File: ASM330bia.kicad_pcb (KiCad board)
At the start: 2 copper layers, 14 x 19.5 mm, 9 parts, among them J1 Conn_01x06_Pin, U1 ASM330LHH

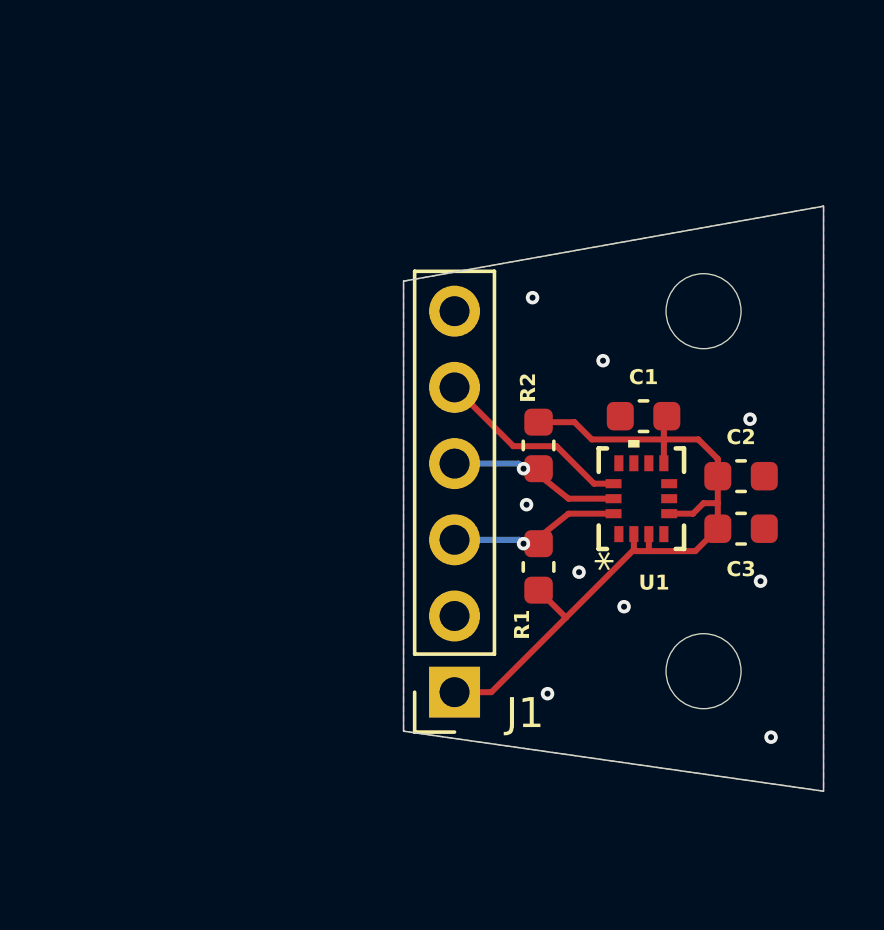
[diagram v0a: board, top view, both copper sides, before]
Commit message: alteração do furo passante
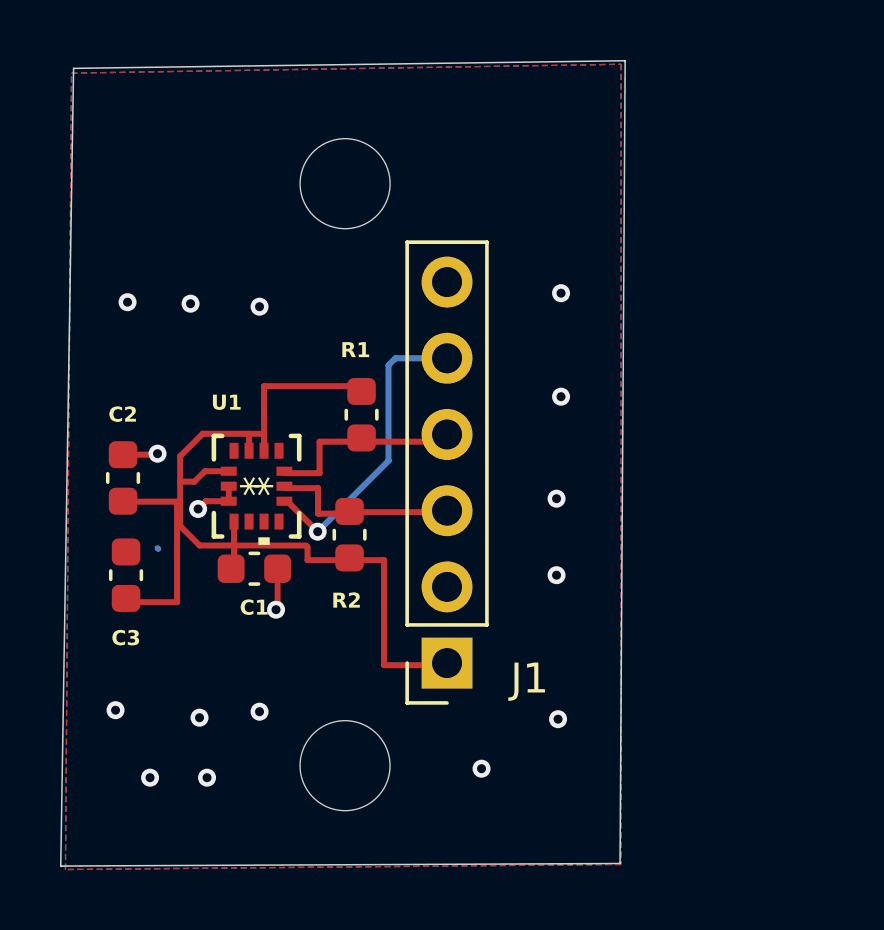
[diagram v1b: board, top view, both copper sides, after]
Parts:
- REF** (x2): value MountingHole_2.5mm -> MountingHole_3mm
- moved C2 20.6 mm to (129.7, 94.6), turned to 90 degrees
- moved C3 20.6 mm to (129.8, 97.8), turned to 90 degrees
- moved C1 13.9 mm to (134.0, 97.6), turned to 0 degrees
- moved U1 12.8 mm to (134.1, 94.8), turned to -90 degrees
- moved REF** 12.7 mm to (137.1, 84.8)
- moved REF** 12.4 mm to (137.1, 104.2)
- moved R1 7.78 mm to (137.6, 92.5), turned to -90 degrees
- moved R2 6.97 mm to (137.2, 96.5), turned to 90 degrees
- moved J1 1.00 mm to (140.4, 100.7)
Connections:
- J1 pad 3: SDA -> SCL
- J1 pad 4: SCL -> SDA
- J1 pad 6: unconnected-(J1-Pin_6-Pad6) -> xshut
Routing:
- net VCC: track 25.7 -> 14.4 mm
- net SCL: track 5.72 -> 0.00 mm, vias 1 -> 0
- net SDA: track 5.70 -> 0.00 mm, vias 1 -> 0
- net GND: track 0.00 -> 4.21 mm, vias 9 -> 17
- net CS: track 6.63 -> 10.1 mm, vias 0 -> 1
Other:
- board size 14 x 19.5 mm -> 18.8 x 26.8 mm

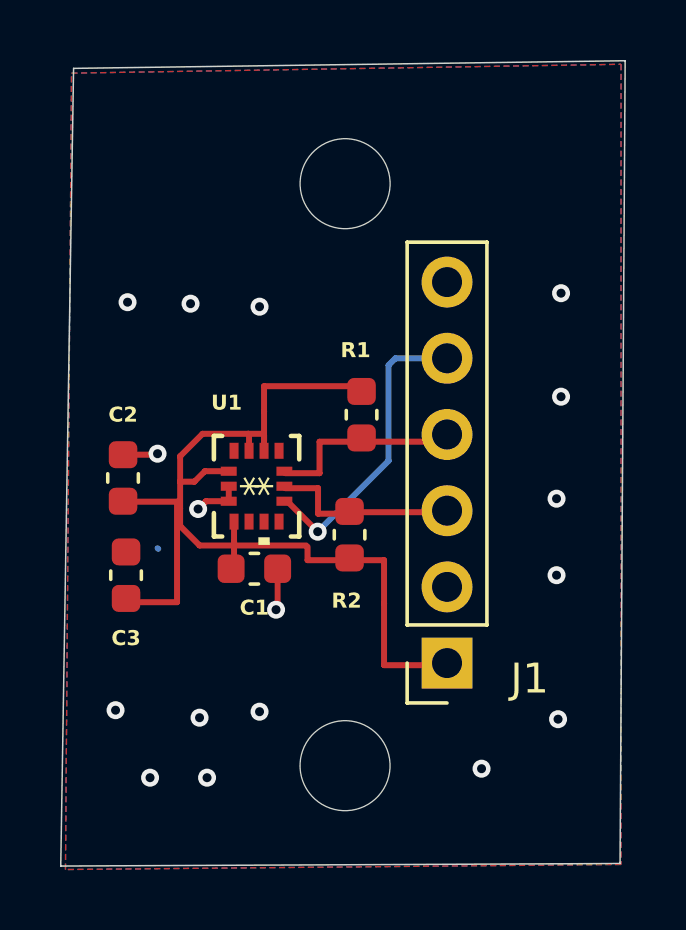
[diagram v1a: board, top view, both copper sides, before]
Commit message: Att
Adicionado interrupts e revisado design pcb e alimentação
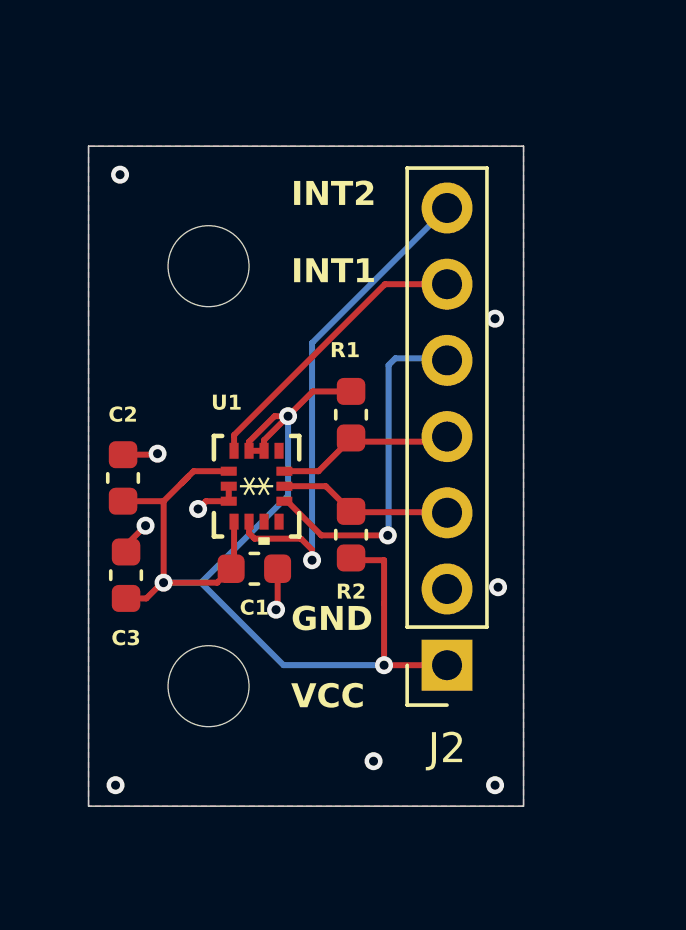
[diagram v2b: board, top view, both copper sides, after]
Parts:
- removed J1: Conn_01x06_Pin, Connector_PinSocket_2.54mm:PinSocket_1x06_P2.54mm_Vertical
- removed REF** (x2): MountingHole_3mm, MountingHole:MountingHole_2.5mm
- added H1: MountingHole, MountingHole:MountingHole_2.7mm, F.Cu at (132.5, 87.5)
- added H2: MountingHole, MountingHole:MountingHole_2.7mm, F.Cu at (132.5, 101.5)
- added J2: Conn_01x07_Pin, Connector_PinSocket_2.54mm:PinSocket_1x07_P2.54mm_Vertical, F.Cu at (140.4, 100.8)
- moved R1 0.35 mm to (137.2, 92.5)
- moved R2 0.05 mm to (137.2, 96.5)
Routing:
- net VCC: track 14.4 -> 34.1 mm, vias 0 -> 3
- net INT2: track 0.00 -> 16.7 mm, vias 0 -> 1
- net INT1: track 0.00 -> 9.71 mm
- net SDA: track 0.00 -> 2.70 mm
- net SCL: track 0.00 -> 2.57 mm
- net CS: track 10.1 -> 11.6 mm
- net GND: track 4.21 -> 5.36 mm, vias 17 -> 10
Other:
- board size 18.8 x 26.8 mm -> 14.5 x 22 mm
- rule pad_to_mask_clearance: 0 -> 0.05
- board text added: "INT2 INT1 CS SDA SCL GND VCC"
- board text added: "INT2 INT1 GND VCC"

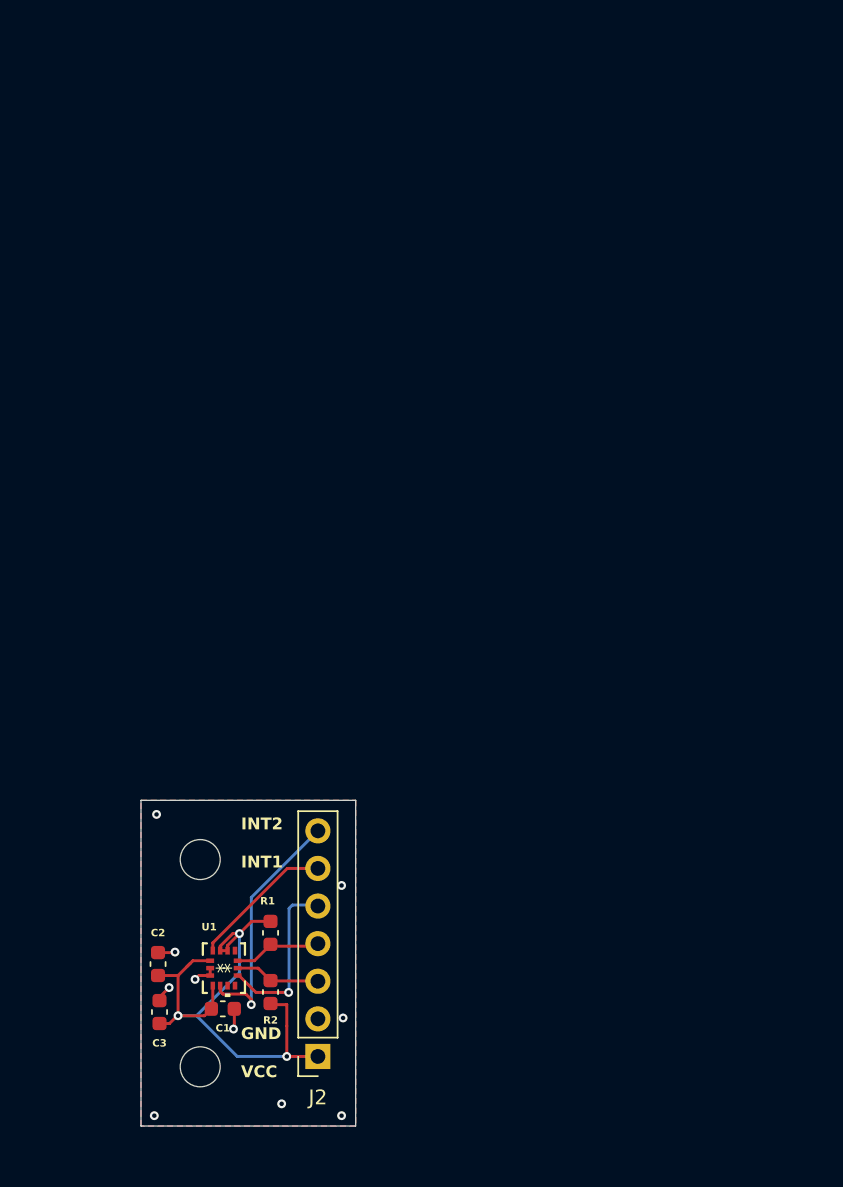
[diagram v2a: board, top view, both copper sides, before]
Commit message: Adição ESP32-S3 e modulo SDCARD
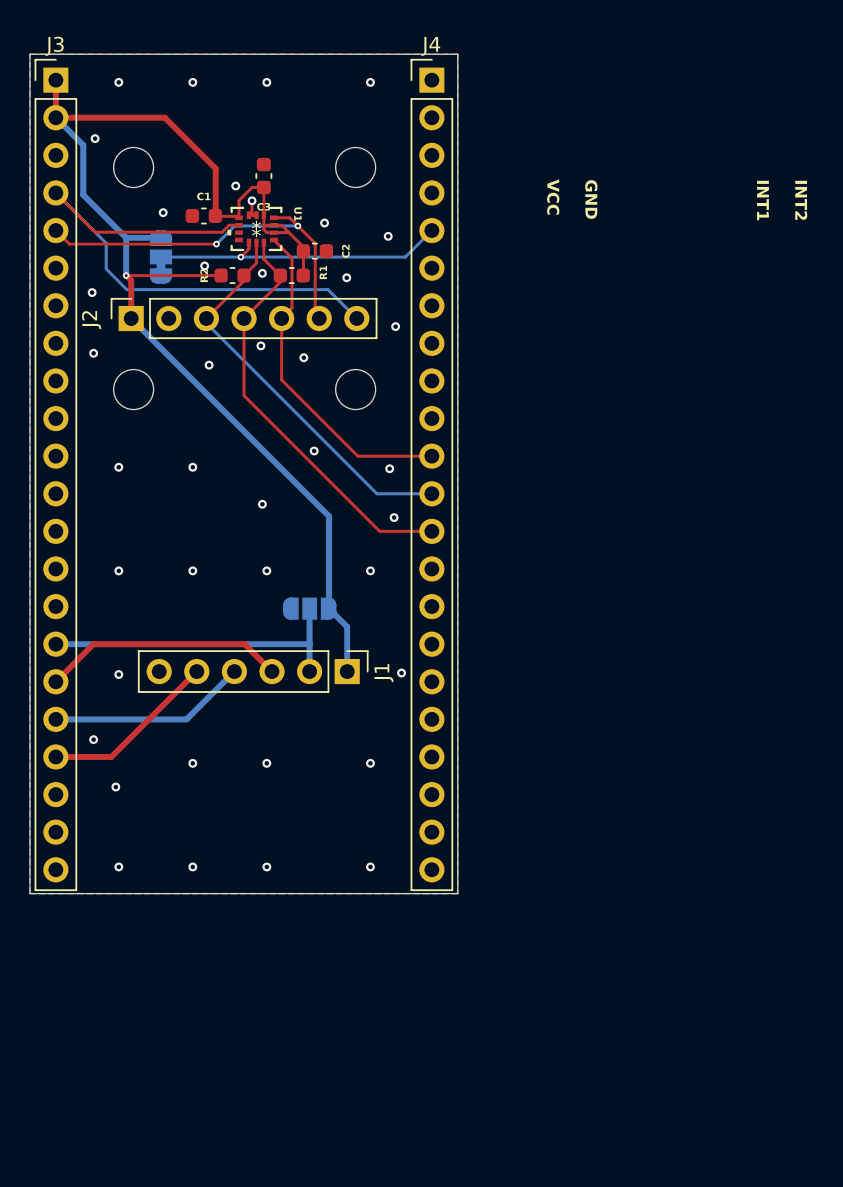
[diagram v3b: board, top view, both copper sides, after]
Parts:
- added H3: MountingHole, MountingHole:MountingHole_2.7mm, F.Cu at (128.0, 40.8)
- added H4: MountingHole, MountingHole:MountingHole_2.7mm, F.Cu at (143.0, 55.8)
- added J1: Conn_01x06_Pin, Connector_PinHeader_2.54mm:PinHeader_1x06_P2.54mm_Vertical, F.Cu at (142.4, 74.8)
- added J3: Conn_01x22_Socket, Connector_PinHeader_2.54mm:PinHeader_1x22_P2.54mm_Vertical, F.Cu at (122.8, 34.9)
- added J4: Conn_01x22_Socket, Connector_PinHeader_2.54mm:PinHeader_1x22_P2.54mm_Vertical, F.Cu at (148.2, 34.9)
- added JP1: SolderJumper_3_Bridged12, Jumper:SolderJumper-3_P1.3mm_Bridged12_RoundedPad1.0x1.5mm, B.Cu at (129.8, 46.8)
- added JP3: SolderJumper_3_Open, Jumper:SolderJumper-3_P1.3mm_Open_RoundedPad1.0x1.5mm, B.Cu at (139.9, 70.5)
- moved C3 56.9 mm to (136.8, 41.3)
- moved C1 53.6 mm to (132.8, 44.0), turned to 180 degrees
- moved J2 51.4 mm to (127.8, 51.0), turned to 90 degrees
- moved U1 50.0 mm to (136.3, 44.9), turned to 180 degrees
- moved C2 49.3 mm to (140.2, 46.4), turned to 0 degrees
- moved R2 48.5 mm to (134.7, 48.0), turned to 0 degrees
- moved H1 47.9 mm to (143.0, 40.8)
- moved H2 46.0 mm to (128.0, 55.8)
- moved R1 44.4 mm to (138.7, 48.0), turned to 180 degrees
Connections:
- net SCL renamed SCL/CLK
- net SDA renamed SDA/MOSI
- J2 pad 5: CS -> SA0/MISO
- U1 pad 1: SA0 -> SA0/MISO
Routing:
- net VCC: track 34.1 -> 87.0 mm, vias 3 -> 1
- net SDA/MOSI: track 2.70 -> 28.3 mm
- net SCL/CLK: track 2.57 -> 26.8 mm
- net SA0/MISO: track 0.00 -> 22.5 mm
- net INT2: track 16.7 -> 38.5 mm, vias 1 -> 0
- net CS-SDCARD: track 0.00 -> 21.2 mm
- net MOSI-SDCARD: track 0.00 -> 16.4 mm
- net INT1: track 9.71 -> 26.0 mm, vias 0 -> 2
- net CLK-SDCARD: track 0.00 -> 13.4 mm
- net MISO-SDCARD: track 0.00 -> 11.9 mm
- net CS: track 11.6 -> 20.3 mm
- net GND: track 5.36 -> 1.51 mm, vias 10 -> 40
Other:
- board size 14.5 x 22 mm -> 28.9 x 56.7 mm
